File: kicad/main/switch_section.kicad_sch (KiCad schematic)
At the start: 30 parts, among them SW4 IMU SET, SW5 GOAL, SW6 START, SW7 AUX1, U10 PCF8574PW, U11 AE-BNO055, U9 AZ1117CH-3.3

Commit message: no message
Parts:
- removed U11: AE-BNO055, 0.main.robot:AE-BNO055, symbol 0.main.robot.library:AE-BNO055
- renumbered C24 to C12, C25 to C13, C26 to C14, C27 to C15, D13 to D15, D14 to D16, D15 to D17, D16 to D18, D17 to D19, D18 to D20, R37 to R32, R38 to R33, R39 to R34, R40 to R35, R41 to R36, R42 to R37, R43 to R38, R44 to R39, R45 to R40, R46 to R41, R47 to R42, R48 to R43, SW4 to SW5, SW5 to SW6, SW6 to SW7, SW7 to SW8, U9 to U8, U10 to U9
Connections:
- net SCL_IMU renamed SCL_I2C1
- net SDA_IMU renamed SDA_I2C1
- no-connect marks 4 -> 2
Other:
- moved on the sheet: D19

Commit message: bus
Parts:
- removed SW5: IMU SET, Button_Switch_THT:SW_Tactile_Straight_KSA0Axx1LFTR, symbol Switch:SW_Push
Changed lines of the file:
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@@
   (junction (at 217.17 154.94) (diameter 0) (color 0 0 0 0)
-  )
-  (junction (at 43.18 184.15) (diameter 0) (color 0 0 0 0)
   )
   (junction (at 71.12 133.35) (diameter 0) (color 0 0 0 0)
@@
     (stroke (width 0) (type default) (color 0 0 0 0))
   )
-  (wire (pts (xy 43.18 161.29) (xy 39.37 161.29))
-    (stroke (width 0) (type default) (color 0 0 0 0))
-  )
   (wire (pts (xy 116.84 101.6) (xy 116.84 115.57))
     (stroke (width 0) (type default) (color 0 0 0 0))
@@
     (stroke (width 0) (type default) (color 0 0 0 0))
   )
-  (wire (pts (xy 39.37 146.05) (xy 34.29 146.05))
-    (stroke (width 0) (type default) (color 0 0 0 0))
-  )
   (wire (pts (xy 71.12 125.73) (xy 71.12 133.35))
     (stroke (width 0) (type default) (color 0 0 0 0))
@@
     (stroke (width 0) (type default) (color 0 0 0 0))
   )
-  (wire (pts (xy 43.18 184.15) (xy 53.34 184.15))
-    (stroke (width 0) (type default) (color 0 0 0 0))
-  )
   (wire (pts (xy 250.19 138.43) (xy 247.65 138.43))
     (stroke (width 0) (type default) (color 0 0 0 0))
@@
     (stroke (width 0) (type default) (color 0 0 0 0))
   )
-  (wire (pts (xy 39.37 161.29) (xy 39.37 146.05))
-    (stroke (width 0) (type default) (color 0 0 0 0))
-  )
   (wire (pts (xy 119.38 88.9) (xy 134.62 88.9))
     (stroke (width 0) (type default) (color 0 0 0 0))
@@
     (stroke (width 0) (type default) (color 0 0 0 0))
   )
-  (wire (pts (xy 43.18 181.61) (xy 43.18 184.15))
-    (stroke (width 0) (type default) (color 0 0 0 0))
-  )
   (wire (pts (xy 76.2 184.15) (xy 53.34 184.15))
     (stroke (width 0) (type default) (color 0 0 0 0))
@@
     (stroke (width 0) (type default) (color 0 0 0 0))
   )
-  (wire (pts (xy 36.83 184.15) (xy 43.18 184.15))
+  (wire (pts (xy 36.83 184.15) (xy 53.34 184.15))
     (stroke (width 0) (type default) (color 0 0 0 0))
   )
@@
   )
   (wire (pts (xy 54.61 135.89) (xy 34.29 135.89))
-    (stroke (width 0) (type default) (color 0 0 0 0))
-  )
-  (wire (pts (xy 43.18 161.29) (xy 43.18 171.45))
     (stroke (width 0) (type default) (color 0 0 0 0))
   )
@@
     (pin "1")
   )
-  (symbol (lib_id "Switch:SW_Push") (at 43.18 176.53 270) (unit 1)
-    (in_bom yes) (on_board yes) (fields_autoplaced)
-    (property "Reference" "SW5" (id 0) (at 46.863 175.6953 90)
-      (effects (font (size 1.27 1.27)) (justify left))
-    )
-    (property "Value" "IMU SET" (id 1) (at 46.863 178.2322 90)
-      (effects (font (size 1.27 1.27)) (justify left))
-    )
-    (property "Footprint" "Button_Switch_THT:SW_Tactile_Straight_KSA0Axx1LFTR" (id 2) (at 48.26 176.53 0)
-      (effects (font (size 1.27 1.27)) hide)
-    )
-    (property "Datasheet" "~" (id 3) (at 48.26 176.53 0)
-      (effects (font (size 1.27 1.27)) hide)
-    )
-    (pin "1")
-    (pin "2")
-  )
   (symbol (lib_id "power:GND") (at 181.61 157.48 0) (mirror y) (unit 1)

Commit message: main bus
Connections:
- no-connect marks 2 -> 3
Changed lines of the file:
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@@
   (no_connect (at 166.37 113.03))
   (no_connect (at 34.29 138.43))
+  (no_connect (at 34.29 146.05))
   (wire (pts (xy 134.62 88.9) (xy 153.67 88.9))
     (stroke (width 0) (type default) (color 0 0 0 0))

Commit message: update
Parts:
- removed D19: RSX101VAM-30, Diode_SMD:D_0805_2012Metric_Pad1.15x1.40mm_HandSolder, symbol Device:D
- renumbered C12 to C10, C13 to C11, C14 to C12, C15 to C13, D15 to D13, D16 to D14, D17 to D15, D18 to D16, D20 to D17, R32 to R31, R33 to R32, R34 to R33, R35 to R34, R36 to R35, R37 to R36, R38 to R37, R39 to R38, R40 to R39, R41 to R40, R42 to R41, R43 to R42, U8 to U7, U9 to U8

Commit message: update: main
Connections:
- net SCL_I2C1 renamed I2C_1.SCL
- net SDA_I2C1 renamed I2C_1.SDA
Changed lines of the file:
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@@
   (junction (at 233.68 88.9) (diameter 0) (color 0 0 0 0)
+  )
+  (junction (at 266.7 123.19) (diameter 0) (color 0 0 0 0)
   )
   (junction (at 209.55 154.94) (diameter 0) (color 0 0 0 0)
@@
   (no_connect (at 34.29 138.43))
   (no_connect (at 34.29 146.05))
+  (bus_entry (at 259.08 118.11) (size -2.54 -2.54)
+    (stroke (width 0) (type default) (color 0 0 0 0))
+  )
+  (bus_entry (at 259.08 123.19) (size -2.54 -2.54)
+    (stroke (width 0) (type default) (color 0 0 0 0))
+  )
   (wire (pts (xy 134.62 88.9) (xy 153.67 88.9))
     (stroke (width 0) (type default) (color 0 0 0 0))
@@
     (stroke (width 0) (type default) (color 0 0 0 0))
   )
-  (wire (pts (xy 240.03 115.57) (xy 265.43 115.57))
+  (wire (pts (xy 240.03 115.57) (xy 256.54 115.57))
     (stroke (width 0) (type default) (color 0 0 0 0))
   )
@@
     (stroke (width 0) (type default) (color 0 0 0 0))
   )
+  (bus (pts (xy 266.7 127) (xy 267.97 127))
+    (stroke (width 0) (type default) (color 0 0 0 0))
+  )
   (wire (pts (xy 80.01 50.8) (xy 153.67 50.8))
     (stroke (width 0) (type default) (color 0 0 0 0))
@@
     (stroke (width 0) (type default) (color 0 0 0 0))
   )
+  (bus (pts (xy 266.7 118.11) (xy 266.7 123.19))
+    (stroke (width 0) (type default) (color 0 0 0 0))
+  )
   (wire (pts (xy 222.25 50.8) (xy 222.25 96.52))
     (stroke (width 0) (type default) (color 0 0 0 0))
@@
     (stroke (width 0) (type default) (color 0 0 0 0))
   )
+  (bus (pts (xy 259.08 118.11) (xy 266.7 118.11))
+    (stroke (width 0) (type default) (color 0 0 0 0))
+  )
+  (bus (pts (xy 266.7 123.19) (xy 266.7 127))
+    (stroke (width 0) (type default) (color 0 0 0 0))
+  )
   (wire (pts (xy 46.99 36.83) (xy 55.88 36.83))
     (stroke (width 0) (type default) (color 0 0 0 0))
@@
     (stroke (width 0) (type default) (color 0 0 0 0))
   )
-  (wire (pts (xy 233.68 120.65) (xy 265.43 120.65))
+  (wire (pts (xy 233.68 120.65) (xy 256.54 120.65))
     (stroke (width 0) (type default) (color 0 0 0 0))
   )
@@
     (stroke (width 0) (type default) (color 0 0 0 0))
   )
+  (bus (pts (xy 259.08 123.19) (xy 266.7 123.19))
+    (stroke (width 0) (type default) (color 0 0 0 0))
+  )
   (wire (pts (xy 119.38 154.94) (xy 119.38 149.86))
     (stroke (width 0) (type default) (color 0 0 0 0))
@@
     (stroke (width 0) (type default) (color 0 0 0 0))
   )
-  (text "SDA" (at 259.08 120.65 180)
+  (text "SDA" (at 255.27 120.65 180)
     (effects (font (size 1.524 1.524)) (justify right bottom))
   )
-  (text "SCL" (at 259.08 115.57 180)
+  (text "SCL" (at 255.27 115.57 180)
     (effects (font (size 1.524 1.524)) (justify right bottom))
   )
   (text "(Switch section)" (at 60.96 125.73 0)
     (effects (font (size 2.54 2.54)) (justify left bottom))
+  )
+  (label "I2C_1.SCL" (at 256.54 115.57 0)
+    (effects (font (size 1.27 1.27)) (justify left bottom))
+  )
+  (label "I2C_1.SDA" (at 256.54 120.65 0)
+    (effects (font (size 1.27 1.27)) (justify left bottom))
   )
   (global_label "SW1_1" (shape input) (at 34.29 135.89 180) (fields_autoplaced)
@@
     )
   )
-  (global_label "SDA_I2C1" (shape input) (at 265.43 120.65 0) (fields_autoplaced)
+  (global_label "I2C_1{I2C_1}" (shape input) (at 267.97 127 0) (fields_autoplaced)
     (effects (font (size 1.27 1.27)) (justify left))
-    (property "Intersheet References" "${INTERSHEET_REFS}" (id 0) (at 276.6726 120.5706 0)
+    (property "Intersheet References" "${INTERSHEET_REFS}" (id 0) (at 282.5993 126.9206 0)
       (effects (font (size 1.27 1.27)) (justify left) hide)
     )
-  )
-  (global_label "SCL_I2C1" (shape input) (at 265.43 115.57 0) (fields_autoplaced)
-    (effects (font (size 1.27 1.27)) (justify left))
-    (property "Intersheet References" "${INTERSHEET_REFS}" (id 0) (at 276.6121 115.4906 0)
-      (effects (font (size 1.27 1.27)) (justify left) hide)
-    )

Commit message: SW-LED changed
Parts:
- R31, R34: value 470 -> 120
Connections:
- net SW1_2: now also R31.1
- net SW1_5: now also R34.2
- net at SW7.4 (KR): now also R31.2; no longer R31.1
- net at U8.14 (P3): no longer R34.2
- net at U8.12 (P2): no longer R31.2
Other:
- moved on the sheet: R31, R34
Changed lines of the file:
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@@
   )
   (no_connect (at 166.37 113.03))
-  (no_connect (at 34.29 138.43))
-  (no_connect (at 34.29 146.05))
+  (no_connect (at 140.97 118.11))
+  (no_connect (at 166.37 100.33))
   (bus_entry (at 259.08 118.11) (size -2.54 -2.54)
     (stroke (width 0) (type default) (color 0 0 0 0))
@@
     (stroke (width 0) (type default) (color 0 0 0 0))
   )
-  (wire (pts (xy 54.61 161.29) (xy 54.61 176.53))
+  (wire (pts (xy 52.07 161.29) (xy 54.61 161.29))
     (stroke (width 0) (type default) (color 0 0 0 0))
   )
@@
     (stroke (width 0) (type default) (color 0 0 0 0))
   )
+  (wire (pts (xy 34.29 146.05) (xy 40.64 146.05))
+    (stroke (width 0) (type default) (color 0 0 0 0))
+  )
   (wire (pts (xy 105.41 130.81) (xy 105.41 154.94))
     (stroke (width 0) (type default) (color 0 0 0 0))
@@
     (stroke (width 0) (type default) (color 0 0 0 0))
   )
+  (wire (pts (xy 40.64 146.05) (xy 40.64 161.29))
+    (stroke (width 0) (type default) (color 0 0 0 0))
+  )
   (wire (pts (xy 46.99 125.73) (xy 71.12 125.73))
     (stroke (width 0) (type default) (color 0 0 0 0))
@@
     (stroke (width 0) (type default) (color 0 0 0 0))
   )
+  (wire (pts (xy 43.18 156.21) (xy 43.18 138.43))
+    (stroke (width 0) (type default) (color 0 0 0 0))
+  )
   (wire (pts (xy 54.61 151.13) (xy 46.99 151.13))
     (stroke (width 0) (type default) (color 0 0 0 0))
@@
     (stroke (width 0) (type default) (color 0 0 0 0))
   )
-  (wire (pts (xy 111.76 171.45) (xy 129.54 171.45))
-    (stroke (width 0) (type default) (color 0 0 0 0))
-  )
   (wire (pts (xy 71.12 148.59) (xy 71.12 158.75))
     (stroke (width 0) (type default) (color 0 0 0 0))
@@
     (stroke (width 0) (type default) (color 0 0 0 0))
   )
-  (wire (pts (xy 129.54 118.11) (xy 140.97 118.11))
-    (stroke (width 0) (type default) (color 0 0 0 0))
-  )
   (wire (pts (xy 153.67 88.9) (xy 233.68 88.9))
     (stroke (width 0) (type default) (color 0 0 0 0))
@@
     (stroke (width 0) (type default) (color 0 0 0 0))
   )
-  (wire (pts (xy 167.64 100.33) (xy 167.64 176.53))
-    (stroke (width 0) (type default) (color 0 0 0 0))
-  )
   (wire (pts (xy 34.29 140.97) (xy 46.99 140.97))
     (stroke (width 0) (type default) (color 0 0 0 0))
@@
     (stroke (width 0) (type default) (color 0 0 0 0))
   )
-  (wire (pts (xy 123.19 176.53) (xy 167.64 176.53))
-    (stroke (width 0) (type default) (color 0 0 0 0))
-  )
   (wire (pts (xy 46.99 50.8) (xy 54.61 50.8))
     (stroke (width 0) (type default) (color 0 0 0 0))
@@
     (stroke (width 0) (type default) (color 0 0 0 0))
   )
-  (wire (pts (xy 129.54 118.11) (xy 129.54 171.45))
-    (stroke (width 0) (type default) (color 0 0 0 0))
-  )
   (wire (pts (xy 134.62 105.41) (xy 140.97 105.41))
     (stroke (width 0) (type default) (color 0 0 0 0))
   )
-  (wire (pts (xy 52.07 171.45) (xy 104.14 171.45))
-    (stroke (width 0) (type default) (color 0 0 0 0))
-  )
   (wire (pts (xy 64.77 133.35) (xy 71.12 133.35))
     (stroke (width 0) (type default) (color 0 0 0 0))
@@
     (stroke (width 0) (type default) (color 0 0 0 0))
   )
-  (wire (pts (xy 166.37 100.33) (xy 167.64 100.33))
-    (stroke (width 0) (type default) (color 0 0 0 0))
-  )
   (wire (pts (xy 64.77 138.43) (xy 76.2 138.43))
     (stroke (width 0) (type default) (color 0 0 0 0))
@@
     (stroke (width 0) (type default) (color 0 0 0 0))
   )
-  (wire (pts (xy 52.07 156.21) (xy 52.07 171.45))
-    (stroke (width 0) (type default) (color 0 0 0 0))
-  )
   (wire (pts (xy 119.38 113.03) (xy 140.97 113.03))
     (stroke (width 0) (type default) (color 0 0 0 0))
@@
     (stroke (width 0) (type default) (color 0 0 0 0))
   )
-  (wire (pts (xy 54.61 176.53) (xy 115.57 176.53))
+  (wire (pts (xy 40.64 161.29) (xy 44.45 161.29))
     (stroke (width 0) (type default) (color 0 0 0 0))
   )
@@
     (stroke (width 0) (type default) (color 0 0 0 0))
   )
+  (wire (pts (xy 44.45 156.21) (xy 43.18 156.21))
+    (stroke (width 0) (type default) (color 0 0 0 0))
+  )
   (wire (pts (xy 46.99 140.97) (xy 46.99 125.73))
     (stroke (width 0) (type default) (color 0 0 0 0))
@@
   )
   (wire (pts (xy 54.61 135.89) (xy 34.29 135.89))
+    (stroke (width 0) (type default) (color 0 0 0 0))
+  )
+  (wire (pts (xy 34.29 138.43) (xy 43.18 138.43))
     (stroke (width 0) (type default) (color 0 0 0 0))
   )
@@
     (pin "3")
   )
-  (symbol (lib_id "Device:R") (at 119.38 176.53 90) (mirror x) (unit 1)
+  (symbol (lib_id "Device:R") (at 48.26 161.29 270) (mirror x) (unit 1)
     (in_bom yes) (on_board yes)
-    (property "Reference" "R34" (id 0) (at 119.38 171.2722 90))
-    (property "Value" "470" (id 1) (at 119.38 173.5836 90))
-    (property "Footprint" "Resistor_SMD:R_0603_1608Metric_Pad0.98x0.95mm_HandSolder" (id 2) (at 119.38 174.752 90)
-      (effects (font (size 1.27 1.27)) hide)
-    )
-    (property "Datasheet" "~" (id 3) (at 119.38 176.53 0)
+    (property "Reference" "R34" (id 0) (at 48.26 166.5478 90))
+    (property "Value" "120" (id 1) (at 48.26 164.2364 90))
+    (property "Footprint" "Resistor_SMD:R_0603_1608Metric_Pad0.98x0.95mm_HandSolder" (id 2) (at 48.26 163.068 90)
+      (effects (font (size 1.27 1.27)) hide)
+    )
+    (property "Datasheet" "~" (id 3) (at 48.26 161.29 0)
       (effects (font (size 1.27 1.27)) hide)
     )
@@
     (pin "2")
   )
-  (symbol (lib_id "Device:R") (at 107.95 171.45 90) (mirror x) (unit 1)
+  (symbol (lib_id "Device:R") (at 48.26 156.21 90) (mirror x) (unit 1)
     (in_bom yes) (on_board yes)
-    (property "Reference" "R31" (id 0) (at 107.95 166.1922 90))
-    (property "Value" "470" (id 1) (at 107.95 168.5036 90))
-    (property "Footprint" "Resistor_SMD:R_0603_1608Metric_Pad0.98x0.95mm_HandSolder" (id 2) (at 107.95 169.672 90)
-      (effects (font (size 1.27 1.27)) hide)
-    )
-    (property "Datasheet" "~" (id 3) (at 107.95 171.45 0)
-      (effects (font (size 1.27 1.27)) hide)
-    )
+    (property "Reference" "R31" (id 0) (at 48.26 150.9522 90))
+    (property "Value" "120" (id 1) (at 48.26 153.2636 90))
+    (property "Footprint" "Resistor_SMD:R_0603_1608Metric_Pad0.98x0.95mm_HandSolder" (id 2) (at 48.26 154.432 90)
+      (effects (font (size 1.27 1.27)) hide)
+    )
+    (property "Datasheet" "~" (id 3) (at 48.26 156.21 0)
+      (effects (font (size 1.27 1.27)) hide)
+    )

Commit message: fix:
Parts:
- renumbered JP1 to JP2, R34 to R32, R32 to R33, R33 to R34
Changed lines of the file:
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@@
   (symbol (lib_id "Device:R") (at 48.26 161.29 270) (mirror x) (unit 1)
     (in_bom yes) (on_board yes)
-    (property "Reference" "R34" (id 0) (at 48.26 166.5478 90))
+    (property "Reference" "R32" (id 0) (at 48.26 166.5478 90))
     (property "Value" "120" (id 1) (at 48.26 164.2364 90))
     (property "Footprint" "Resistor_SMD:R_0603_1608Metric_Pad0.98x0.95mm_HandSolder" (id 2) (at 48.26 163.068 90)
@@
   (symbol (lib_id "power:GND") (at 53.34 186.69 0) (mirror y) (unit 1)
     (in_bom yes) (on_board yes)
-    (property "Reference" "#PWR062" (id 0) (at 53.34 193.04 0)
+    (property "Reference" "#PWR060" (id 0) (at 53.34 193.04 0)
       (effects (font (size 1.27 1.27)) hide)
     )
@@
   (symbol (lib_id "Device:R") (at 113.03 95.25 0) (unit 1)
     (in_bom yes) (on_board yes)
-    (property "Reference" "R32" (id 0) (at 114.808 94.0816 0)
+    (property "Reference" "R33" (id 0) (at 114.808 94.0816 0)
       (effects (font (size 1.27 1.27)) (justify left))
     )
@@
   (symbol (lib_id "Device:R") (at 119.38 95.25 0) (unit 1)
     (in_bom yes) (on_board yes)
-    (property "Reference" "R33" (id 0) (at 121.158 94.0816 0)
+    (property "Reference" "R34" (id 0) (at 121.158 94.0816 0)
       (effects (font (size 1.27 1.27)) (justify left))
     )
@@
   (symbol (lib_id "Jumper:Jumper_2_Bridged") (at 222.25 101.6 270) (unit 1)
     (in_bom yes) (on_board yes)
-    (property "Reference" "JP1" (id 0) (at 227.203 101.6 0))
+    (property "Reference" "JP2" (id 0) (at 227.203 101.6 0))
     (property "Value" "Jumper_2_Bridged" (id 1) (at 224.8916 101.6 0))
     (property "Footprint" "Connector_PinHeader_1.27mm:PinHeader_1x02_P1.27mm_Vertical" (id 2) (at 222.25 101.6 0)
@@
   (symbol (lib_id "power:+5V") (at 55.88 36.83 270) (unit 1)
     (in_bom yes) (on_board yes)
-    (property "Reference" "#PWR063" (id 0) (at 52.07 36.83 0)
+    (property "Reference" "#PWR061" (id 0) (at 52.07 36.83 0)
       (effects (font (size 1.27 1.27)) hide)
     )
@@
   (symbol (lib_id "power:GND") (at 62.23 67.31 0) (unit 1)
     (in_bom yes) (on_board yes) (fields_autoplaced)
-    (property "Reference" "#PWR064" (id 0) (at 62.23 73.66 0)
+    (property "Reference" "#PWR062" (id 0) (at 62.23 73.66 0)
       (effects (font (size 1.27 1.27)) hide)
     )
@@
   (symbol (lib_id "power:GND") (at 181.61 157.48 0) (mirror y) (unit 1)
     (in_bom yes) (on_board yes)
-    (property "Reference" "#PWR065" (id 0) (at 181.61 163.83 0)
+    (property "Reference" "#PWR063" (id 0) (at 181.61 163.83 0)
       (effects (font (size 1.27 1.27)) hide)
     )
@@
   (symbol (lib_id "power:GND") (at 250.19 156.21 0) (mirror y) (unit 1)
     (in_bom yes) (on_board yes)
-    (property "Reference" "#PWR066" (id 0) (at 250.19 162.56 0)
-      (effects (font (size 1.27 1.27)) hide)
-    )
+    (property "Reference" "#PWR064" (id 0) (at 250.19 162.56 0)
+      (effects (font (size 1.27 1.27)) hide)
+    )

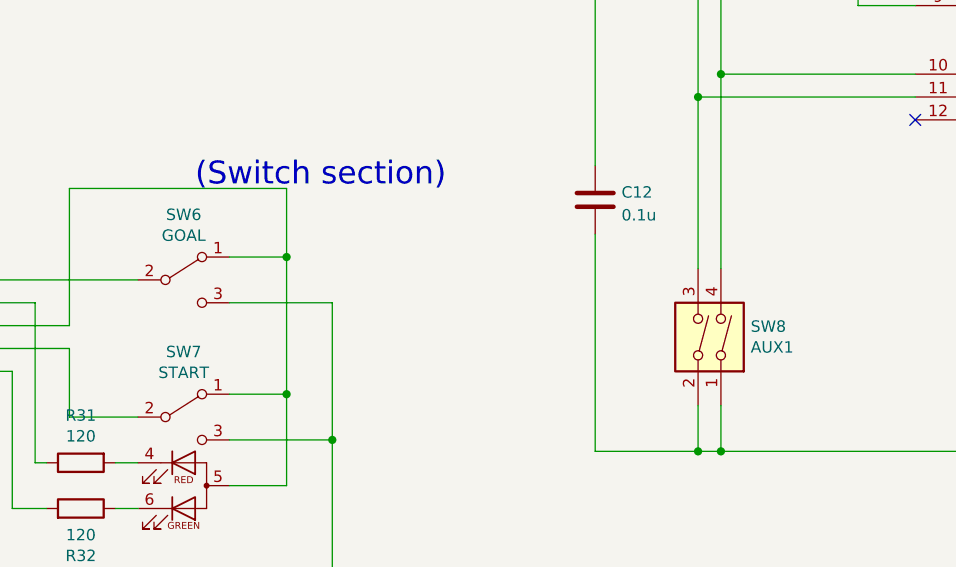
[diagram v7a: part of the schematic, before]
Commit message: fix: vison-board GND
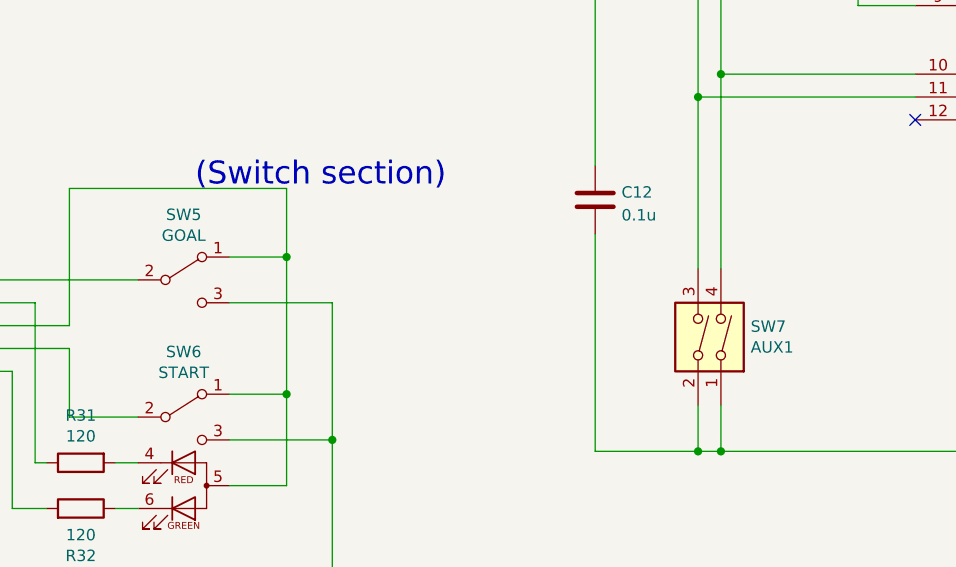
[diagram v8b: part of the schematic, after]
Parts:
- renumbered SW6 to SW5, SW7 to SW6, SW8 to SW7
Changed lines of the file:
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@@
   (symbol (lib_id "0.main.robot.library:SW_NKK_B-12CCPRM") (at 59.69 156.21 0) (unit 1)
     (in_bom yes) (on_board yes)
-    (property "Reference" "SW7" (id 0) (at 59.69 143.891 0))
+    (property "Reference" "SW6" (id 0) (at 59.69 143.891 0))
     (property "Value" "START" (id 1) (at 59.69 146.2024 0))
     (property "Footprint" "0.main.robot:SW_NKK_B-12CCPRM" (id 2) (at 59.69 144.78 0)
@@
   (symbol (lib_id "Switch:SW_SPDT") (at 59.69 135.89 0) (unit 1)
     (in_bom yes) (on_board yes)
-    (property "Reference" "SW6" (id 0) (at 59.69 128.651 0))
+    (property "Reference" "SW5" (id 0) (at 59.69 128.651 0))
     (property "Value" "GOAL" (id 1) (at 59.69 130.9624 0))
     (property "Footprint" "0.main.robot:MFS101D-14-Z" (id 2) (at 59.69 135.89 0)
@@
   (symbol (lib_id "power:GND") (at 53.34 186.69 0) (mirror y) (unit 1)
     (in_bom yes) (on_board yes)
-    (property "Reference" "#PWR060" (id 0) (at 53.34 193.04 0)
+    (property "Reference" "#PWR059" (id 0) (at 53.34 193.04 0)
       (effects (font (size 1.27 1.27)) hide)
     )
@@
   (symbol (lib_id "Switch:SW_DIP_x02") (at 116.84 142.24 270) (mirror x) (unit 1)
     (in_bom yes) (on_board yes)
-    (property "Reference" "SW8" (id 0) (at 122.682 141.0716 90)
+    (property "Reference" "SW7" (id 0) (at 122.682 141.0716 90)
       (effects (font (size 1.27 1.27)) (justify left))
     )
@@
   (symbol (lib_id "power:+5V") (at 55.88 36.83 270) (unit 1)
     (in_bom yes) (on_board yes)
-    (property "Reference" "#PWR061" (id 0) (at 52.07 36.83 0)
+    (property "Reference" "#PWR060" (id 0) (at 52.07 36.83 0)
       (effects (font (size 1.27 1.27)) hide)
     )
@@
   (symbol (lib_id "power:GND") (at 62.23 67.31 0) (unit 1)
     (in_bom yes) (on_board yes) (fields_autoplaced)
-    (property "Reference" "#PWR062" (id 0) (at 62.23 73.66 0)
+    (property "Reference" "#PWR061" (id 0) (at 62.23 73.66 0)
       (effects (font (size 1.27 1.27)) hide)
     )
@@
   (symbol (lib_id "power:GND") (at 181.61 157.48 0) (mirror y) (unit 1)
     (in_bom yes) (on_board yes)
-    (property "Reference" "#PWR063" (id 0) (at 181.61 163.83 0)
+    (property "Reference" "#PWR062" (id 0) (at 181.61 163.83 0)
       (effects (font (size 1.27 1.27)) hide)
     )
@@
   (symbol (lib_id "power:GND") (at 250.19 156.21 0) (mirror y) (unit 1)
     (in_bom yes) (on_board yes)
-    (property "Reference" "#PWR064" (id 0) (at 250.19 162.56 0)
-      (effects (font (size 1.27 1.27)) hide)
-    )
+    (property "Reference" "#PWR063" (id 0) (at 250.19 162.56 0)
+      (effects (font (size 1.27 1.27)) hide)
+    )
